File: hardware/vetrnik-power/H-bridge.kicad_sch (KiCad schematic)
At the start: 52 parts, among them J10 AC1, J11 AC2, J12 G #Q3, J13 G #Q4, J6 DC IN, J7 PE, J8 G #Q1, J9 G #Q2, Q8 BC846, U7 LM393, U8 IR2104, U9 IR2104

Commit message: [hardware] Add info about hardware mods
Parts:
- removed D1: 1.5KE200CA, Diode_THT:D_DO-201AE_P15.24mm_Horizontal, symbol Diode:1.5KExxCA
- added D1: 1.5KE150A, Diode_THT:D_DO-201AE_P15.24mm_Horizontal, symbol Diode:1.5KExxA
- added R49: 22k, Resistor_SMD:R_1206_3216Metric_Pad1.30x1.75mm_HandSolder, symbol Device:R
- C12, C13, C15, C16, C17, C18, D2, D4, R31, R32, R33, R34, R36, R37, R38, U8, U9: now not fitted
- R35: value 10 -> 10 / 0.5W
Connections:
- net DC+: now also D1.1 (A1)
- net DC-: now also D1.2 (A2)
- net GNDPWR: now also R49.2
- net at R25.2, R26.1, R29.2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: now also R49.1
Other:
- note added: "2024-03 mod: DNP components moved to vetrnik-H-bridge"
- note added: "OVP should trip at 128V (standoff voltage of 1.5KE150A) See OVP-hysteresis.ods (128V ... 4.09V) 109V ... 3.49V 56V ... 1.79V WARNING: +12VP is UNREGULATED 12V!"
- note added: "TODO add extra filtering caps?"
- note added: "TODO improve RC snubber design?"
- note added: "mod: 5-pin connector for vetrnik-H-bridge: +12P, IN1, ~{SD}, IN2, GNDPWR"
- note added: "mod: added R49 instead of making R26 10k"
- note removed: "OVP should trip at 180 V 178.5 V ... 5.70 V 90.8 V ... 2.90 V"
- note removed: "TODO RC snubber design"
- note removed: "TODO calculate filtering caps"
- note removed: "TODO s/22u/10u/ ??"
- note removed: "UF400x diodes are much faster than 1N400x"

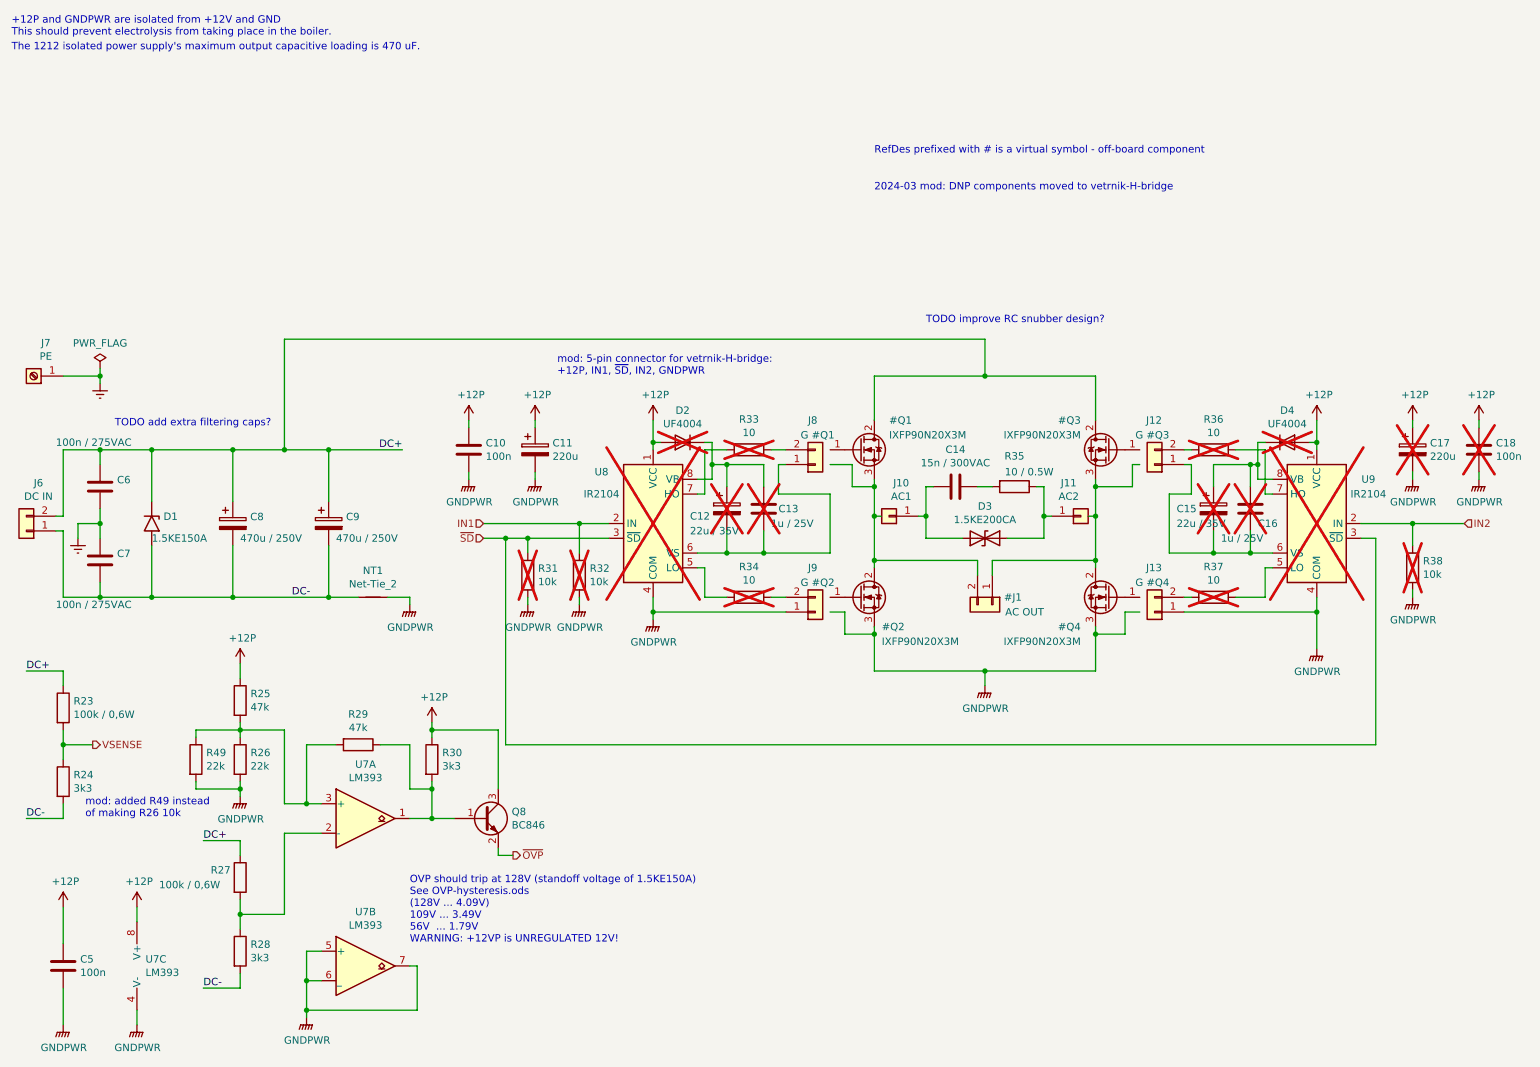
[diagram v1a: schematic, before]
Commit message: [hardware] Clean up vetrnik-power schematic
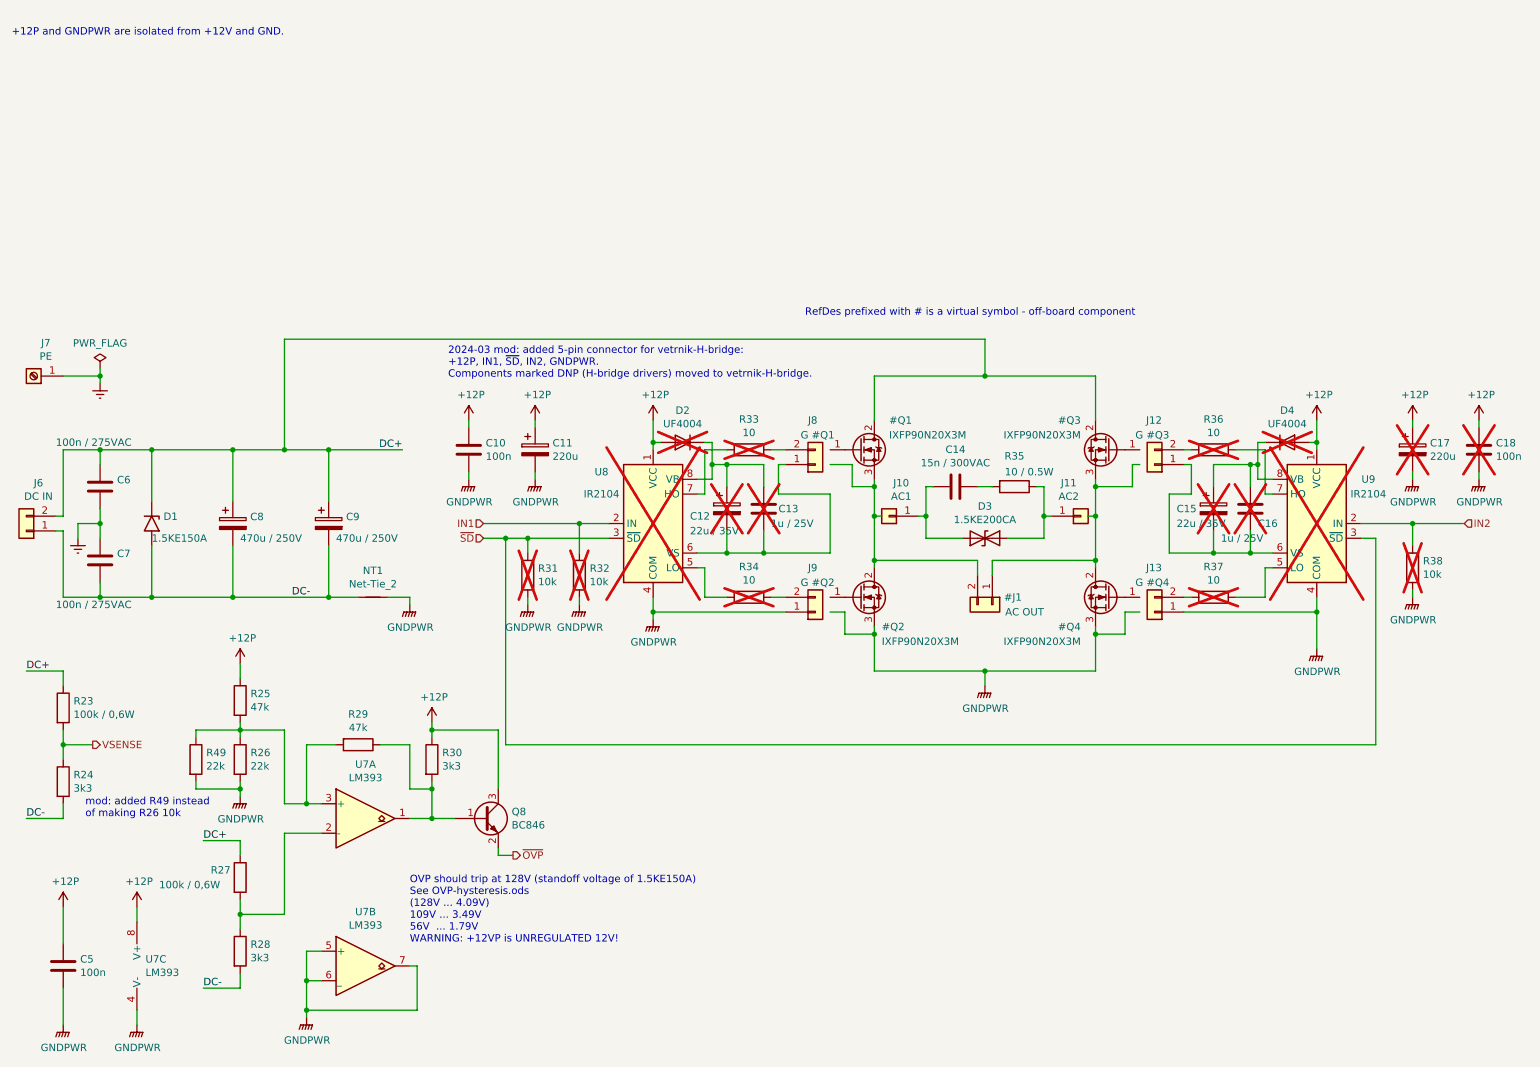
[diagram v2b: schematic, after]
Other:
- note added: "+12P and GNDPWR are isolated from +12V and GND."
- note added: "2024-03 mod: added 5-pin connector for vetrnik-H-bridge: +12P, IN1, ~{SD}, IN2, GNDPWR. Components marked DNP (H-bridge drivers) moved to vetrnik-H-bridge."
- note removed: "+12P and GNDPWR are isolated from +12V and GND This should prevent electrolysis from taking place in the boiler."
- note removed: "2024-03 mod: DNP components moved to vetrnik-H-bridge"
- note removed: "TODO add extra filtering caps?"
- note removed: "TODO improve RC snubber design?"
- note removed: "The 1212 isolated power supply's maximum output capacitive loading is 470 uF."
- note removed: "mod: 5-pin connector for vetrnik-H-bridge: +12P, IN1, ~{SD}, IN2, GNDPWR"
- company: (none) -> Ondřej Sluka
- title: (none) -> vetrnik-power H-bridge
